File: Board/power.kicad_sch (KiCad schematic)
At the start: 6 parts, among them J1 Conn_01x02, U1 OKI-78SR-3.3_1.5-W36H-C

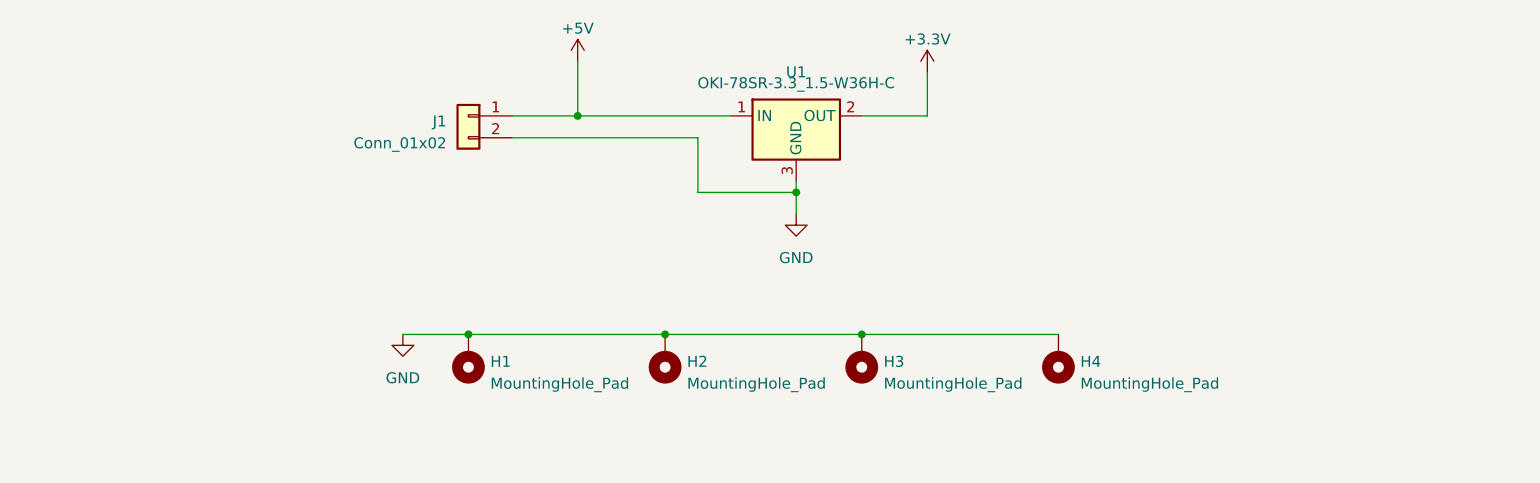
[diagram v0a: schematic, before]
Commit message: make power circuit from 120v mains
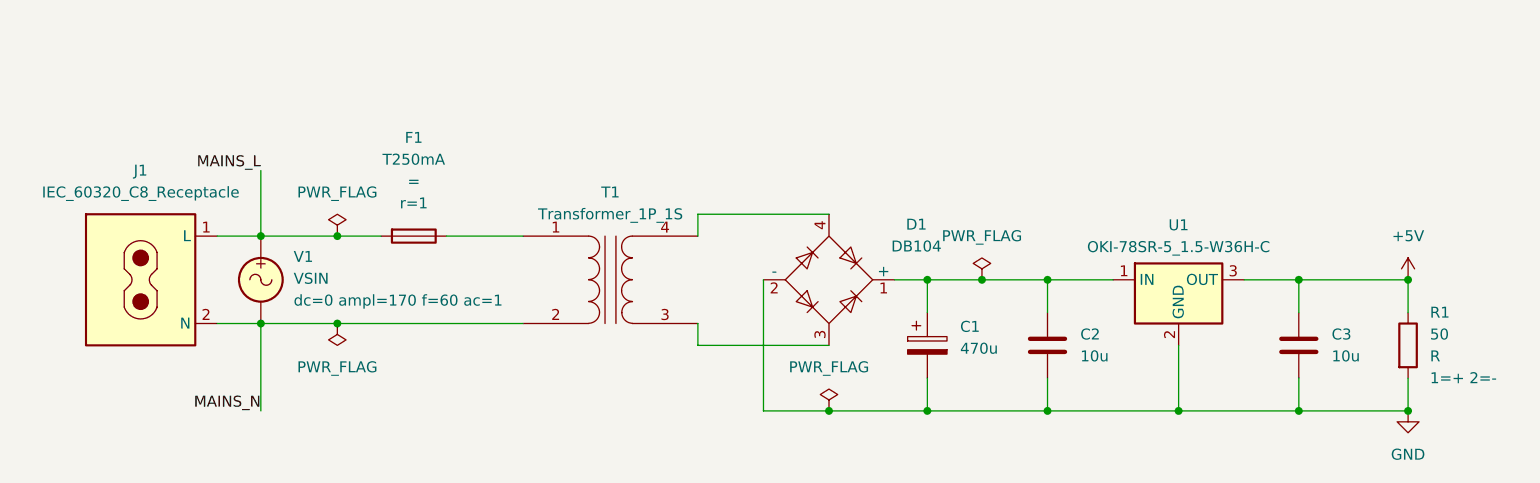
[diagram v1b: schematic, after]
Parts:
- removed H1, H2, H3, H4: MountingHole_Pad, MountingHole:MountingHole_2.5mm_Pad, symbol Mechanical:MountingHole_Pad
- removed J1: Conn_01x02, Connector_JST:JST_XH_B2B-XH-AM_1x02_P2.50mm_Vertical, symbol Connector_Generic:Conn_01x02
- removed U1: OKI-78SR-3.3_1.5-W36H-C, Converter_DCDC:Converter_DCDC_Murata_OKI-78SR_Horizontal, symbol Converter_DCDC:OKI-78SR-3.3_1.5-W36H-C
- added C1: 470u, symbol Device:C_Polarized
- added C2, C3: 10u, symbol Device:C
- added D1: DB104, Diode_THT:Diode_Bridge_DIP-4_W7.62mm_P5.08mm, symbol Diode_Bridge:DF04M
- added F1: T250mA, symbol Device:Fuse
- added J1: IEC_60320_C8_Receptacle, symbol Connector:IEC_60320_C8_Receptacle
- added R1: 50, symbol Device:R
- added T1: Transformer_1P_1S, symbol Device:Transformer_1P_1S
- added U1: OKI-78SR-5_1.5-W36H-C, Converter_DCDC:Converter_DCDC_Murata_OKI-78SR_Horizontal, symbol Converter_DCDC:OKI-78SR-5_1.5-W36H-C
- added V1: VSIN, symbol Simulation_SPICE:VSIN
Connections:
- net +5V: now also C3.1, R1.1, U1.3 (OUT)
- net GND: now also C1.2, C2.2, C3.2, D1.2 (-), R1.2, U1.2 (GND)
- new net: C1.1, C2.1, D1.1 (+), U1.1 (IN)
- new net: D1.3, T1.3 (SA)
- new net: D1.4, T1.4 (SB)
- new net: F1.1, T1.1 (AA)
- new net MAINS_L: F1.2, J1.1 (L), V1.1
- new net MAINS_N: J1.2 (N), T1.2 (AB), V1.2

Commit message: start work on clock
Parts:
- R1: value 50 -> 100k; now in the parts list
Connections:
- net +5V: no longer R1.1
- net GND: no longer R1.2
- net at D1.4, T1.4 (SB): now also R1.2
- new net AC_SENSE: R1.1
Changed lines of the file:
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@@
+	)
+	(junction
+		(at 95.25 54.61)
+		(diameter 0)
+		(color 0 0 0 0)
 	)
 	(junction
@@
 	)
 	(junction
-		(at 172.72 77.47)
-		(diameter 0)
-		(color 0 0 0 0)
-	)
-	(junction
 		(at 160.02 62.23)
 		(diameter 0)
@@
 	)
 	(junction
-		(at 172.72 62.23)
-		(diameter 0)
-		(color 0 0 0 0)
-	)
-	(junction
 		(at 48.26 67.31)
 		(diameter 0)
@@
 	(wire
 		(pts
+			(xy 95.25 54.61) (xy 105.41 54.61)
+		)
+		(stroke
+			(width 0)
+			(type default)
+		)
+	)
+	(wire
+		(pts
 			(xy 90.17 69.85) (xy 105.41 69.85)
 		)
@@
 	(wire
 		(pts
-			(xy 172.72 66.04) (xy 172.72 62.23)
-		)
-		(stroke
-			(width 0)
-			(type default)
-		)
-	)
-	(wire
-		(pts
 			(xy 116.84 62.23) (xy 123.19 62.23)
 		)
@@
 	(wire
 		(pts
-			(xy 90.17 54.61) (xy 105.41 54.61)
+			(xy 90.17 54.61) (xy 95.25 54.61)
 		)
 		(stroke
@@
 	(wire
 		(pts
+			(xy 95.25 44.45) (xy 95.25 41.91)
+		)
+		(stroke
+			(width 0)
+			(type default)
+		)
+	)
+	(wire
+		(pts
 			(xy 146.05 77.47) (xy 160.02 77.47)
 		)
@@
 	(wire
 		(pts
-			(xy 172.72 73.66) (xy 172.72 77.47)
-		)
-		(stroke
-			(width 0)
-			(type default)
-		)
-	)
-	(wire
-		(pts
 			(xy 39.37 49.53) (xy 39.37 57.15)
 		)
@@
 	(wire
 		(pts
+			(xy 95.25 41.91) (xy 99.06 41.91)
+		)
+		(stroke
+			(width 0)
+			(type default)
+		)
+	)
+	(wire
+		(pts
 			(xy 39.37 67.31) (xy 48.26 67.31)
 		)
@@
 		(pts
 			(xy 130.81 73.66) (xy 130.81 77.47)
+		)
+		(stroke
+			(width 0)
+			(type default)
+		)
+	)
+	(wire
+		(pts
+			(xy 95.25 52.07) (xy 95.25 54.61)
 		)
 		(stroke
@@
 			)
 			(justify right bottom)
+		)
+	)
+	(hierarchical_label "AC_SENSE"
+		(shape output)
+		(at 99.06 41.91 0)
+		(effects
+			(font
+				(size 1.27 1.27)
+			)
+			(justify left)
 		)
 	)
@@
 	)
 	(symbol
+		(lib_id "Device:R")
+		(at 95.25 48.26 0)
+		(unit 1)
+		(exclude_from_sim no)
+		(in_bom yes)
+		(on_board yes)
+		(dnp no)
+		(fields_autoplaced yes)
+		(property "Reference" "R1"
+			(at 97.79 46.9899 0)
+			(effects
+				(font
+					(size 1.27 1.27)
+				)
+				(justify left)
+			)
+		)
+		(property "Value" "100k"
+			(at 97.79 49.5299 0)
+			(effects
+				(font
+					(size 1.27 1.27)
+				)
+				(justify left)
+			)
+		)
+		(property "Footprint" ""
+			(at 93.472 48.26 90)
+			(effects
+				(font
+					(size 1.27 1.27)
+				)
+				(hide yes)
+			)
+		)
+		(property "Datasheet" "~"
+			(at 95.25 48.26 0)
+			(effects
+				(font
+					(size 1.27 1.27)
+				)
+				(hide yes)
+			)
+		)
+		(property "Description" "Resistor"
+			(at 95.25 48.26 0)
+			(effects
+				(font
+					(size 1.27 1.27)
+				)
+				(hide yes)
+			)
+		)
+		(pin "2"
+		)
+		(pin "1"
+		)
+		(instances
+			(project ""
+				(path "/4c64ecad-5542-463c-9546-c9b2e3a763b0/35c0af92-b8b1-4456-9e25-6a6ac0397932"
+					(reference "R1")
+					(unit 1)
+				)
+			)
+		)
+	)
+	(symbol
 		(lib_id "Simulation_SPICE:VSIN")
 		(at 39.37 62.23 0)
@@
 					(unit 1)
 				)
-			)
-		)
-	)
-	(symbol
-		(lib_id "Device:R")
-		(at 172.72 69.85 0)
-		(unit 1)
-		(exclude_from_sim no)
-		(in_bom no)
-		(on_board no)
-		(dnp no)
-		(fields_autoplaced yes)
-		(property "Reference" "R1"
-			(at 175.26 66.0399 0)
-			(effects
-				(font
-					(size 1.27 1.27)
-				)
-				(justify left)
-			)
-		)
-		(property "Value" "50"
-			(at 175.26 68.5799 0)
-			(effects
-				(font
-					(size 1.27 1.27)
-				)
-				(justify left)
-			)
-		)
-		(property "Footprint" ""
-			(at 170.942 69.85 90)
-			(effects
-				(font
-					(size 1.27 1.27)
-				)
-				(hide yes)
-			)
-		)
-		(property "Datasheet" "~"
-			(at 172.72 69.85 0)
-			(effects
-				(font
-					(size 1.27 1.27)
-				)
-				(hide yes)
-			)
-		)
-		(property "Description" "Resistor"
-			(at 172.72 69.85 0)
-			(effects
-				(font
-					(size 1.27 1.27)
-				)
-				(hide yes)
-			)
-		)
-		(property "Sim.Device" "R"
-			(at 175.26 71.1199 0)
-			(effects
-				(font
-					(size 1.27 1.27)
-				)
-				(justify left)
-			)
-		)
-		(property "Sim.Pins" "1=+ 2=-"
-			(at 175.26 73.6599 0)
-			(effects
-				(font
-					(size 1.27 1.27)
-				)
-				(justify left)
-			)
-		)
-		(pin "1"
-		)
-		(pin "2"
-		)
-		(instances
-			(project "binary_clock"
-				(path "/4c64ecad-5542-463c-9546-c9b2e3a763b0/35c0af92-b8b1-4456-9e25-6a6ac0397932"
-					(reference "R1")
-					(unit 1)
-				)
